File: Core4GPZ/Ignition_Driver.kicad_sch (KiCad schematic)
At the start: 10 parts, among them Q1 IRG4PF50W, Q2 IRG4PF50W

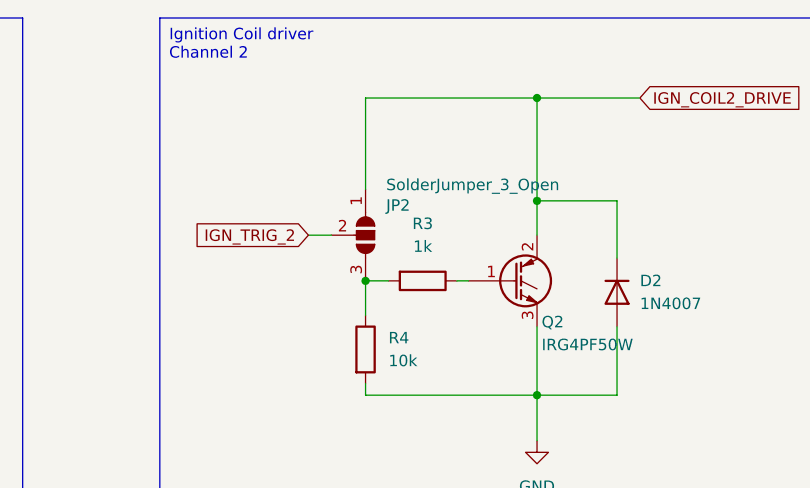
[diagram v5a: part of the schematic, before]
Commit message: Started Implementation of VR Conditionner
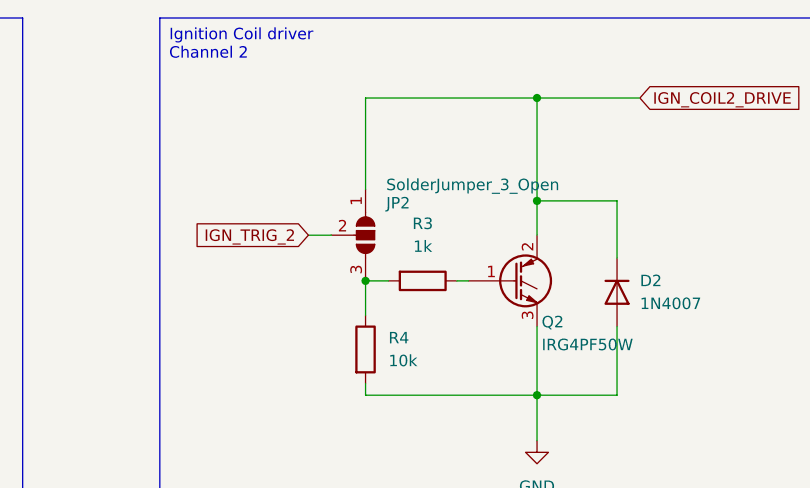
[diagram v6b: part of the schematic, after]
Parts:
- JP1, JP2: footprint (none) -> Jumper:SolderJumper-3_P1.3mm_Open_RoundedPad1.0x1.5mm
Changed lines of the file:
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@@
+	)
+	(junction
+		(at 154.94 60.96)
+		(diameter 0)
+		(color 0 0 0 0)
 	)
 	(junction
@@
 	(junction
 		(at 173.99 73.66)
-		(diameter 0)
-		(color 0 0 0 0)
-	)
-	(junction
-		(at 154.94 60.96)
 		(diameter 0)
 		(color 0 0 0 0)
@@
 	)
 	(symbol
-		(lib_id "Jumper:SolderJumper_3_Open")
-		(at 154.94 55.88 270)
-		(unit 1)
-		(exclude_from_sim yes)
-		(in_bom no)
-		(on_board yes)
-		(dnp no)
-		(property "Reference" "JP2"
-			(at 157.226 52.578 90)
-			(effects
-				(font
-					(size 1.27 1.27)
-				)
-				(justify left)
-			)
-		)
-		(property "Value" "SolderJumper_3_Open"
-			(at 157.226 50.292 90)
-			(effects
-				(font
-					(size 1.27 1.27)
-				)
-				(justify left)
-			)
-		)
-		(property "Footprint" ""
-			(at 154.94 55.88 0)
-			(effects
-				(font
-					(size 1.27 1.27)
-				)
-				(hide yes)
-			)
-		)
-		(property "Datasheet" "~"
-			(at 154.94 55.88 0)
-			(effects
-				(font
-					(size 1.27 1.27)
-				)
-				(hide yes)
-			)
-		)
-		(property "Description" "Solder Jumper, 3-pole, open"
-			(at 154.94 55.88 0)
-			(effects
-				(font
-					(size 1.27 1.27)
-				)
-				(hide yes)
-			)
-		)
-		(pin "3"
-		)
-		(pin "2"
-		)
-		(pin "1"
-		)
-		(instances
-			(project "Core4GPZ"
-				(path "/ac28f42d-34b3-4fcc-84dd-ab6106f99610/d5427090-fd08-4b35-ae6e-bc2a7b0d4087"
-					(reference "JP2")
-					(unit 1)
-				)
-			)
-		)
-	)
-	(symbol
 		(lib_id "power:GND")
 		(at 173.99 78.74 0)
@@
 	(symbol
 		(lib_id "Jumper:SolderJumper_3_Open")
+		(at 154.94 55.88 270)
+		(unit 1)
+		(exclude_from_sim yes)
+		(in_bom no)
+		(on_board yes)
+		(dnp no)
+		(property "Reference" "JP2"
+			(at 157.226 52.324 90)
+			(effects
+				(font
+					(size 1.27 1.27)
+				)
+				(justify left)
+			)
+		)
+		(property "Value" "SolderJumper_3_Open"
+			(at 157.226 50.292 90)
+			(effects
+				(font
+					(size 1.27 1.27)
+				)
+				(justify left)
+			)
+		)
+		(property "Footprint" "Jumper:SolderJumper-3_P1.3mm_Open_RoundedPad1.0x1.5mm"
+			(at 154.94 55.88 0)
+			(effects
+				(font
+					(size 1.27 1.27)
+				)
+				(hide yes)
+			)
+		)
+		(property "Datasheet" "~"
+			(at 154.94 55.88 0)
+			(effects
+				(font
+					(size 1.27 1.27)
+				)
+				(hide yes)
+			)
+		)
+		(property "Description" "Solder Jumper, 3-pole, open"
+			(at 154.94 55.88 0)
+			(effects
+				(font
+					(size 1.27 1.27)
+				)
+				(hide yes)
+			)
+		)
+		(pin "3"
+		)
+		(pin "2"
+		)
+		(pin "1"
+		)
+		(instances
+			(project "Core4GPZ"
+				(path "/ac28f42d-34b3-4fcc-84dd-ab6106f99610/d5427090-fd08-4b35-ae6e-bc2a7b0d4087"
+					(reference "JP2")
+					(unit 1)
+				)
+			)
+		)
+	)
+	(symbol
+		(lib_id "Jumper:SolderJumper_3_Open")
 		(at 69.85 55.88 270)
 		(unit 1)
@@
 			)
 		)
-		(property "Footprint" ""
+		(property "Footprint" "Jumper:SolderJumper-3_P1.3mm_Open_RoundedPad1.0x1.5mm"
 			(at 69.85 55.88 0)
 			(effects

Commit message: Tiny modification
???
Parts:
- D1, D2: footprint Diode_THT:D_DO-41_SOD81_P2.54mm_Vertical_KathodeUp -> Diode_THT:D_DO-41_SOD81_P7.62mm_Horizontal
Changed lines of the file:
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@@
+	)
+	(symbol
+		(lib_id "Device:D")
+		(at 182.88 62.23 270)
+		(unit 1)
+		(exclude_from_sim no)
+		(in_bom yes)
+		(on_board yes)
+		(dnp no)
+		(fields_autoplaced yes)
+		(property "Reference" "D2"
+			(at 185.42 60.9599 90)
+			(effects
+				(font
+					(size 1.27 1.27)
+				)
+				(justify left)
+			)
+		)
+		(property "Value" "1N4007"
+			(at 185.42 63.4999 90)
+			(effects
+				(font
+					(size 1.27 1.27)
+				)
+				(justify left)
+			)
+		)
+		(property "Footprint" "Diode_THT:D_DO-41_SOD81_P7.62mm_Horizontal"
+			(at 182.88 62.23 0)
+			(effects
+				(font
+					(size 1.27 1.27)
+				)
+				(hide yes)
+			)
+		)
+		(property "Datasheet" "~"
+			(at 182.88 62.23 0)
+			(effects
+				(font
+					(size 1.27 1.27)
+				)
+				(hide yes)
+			)
+		)
+		(property "Description" ""
+			(at 182.88 62.23 0)
+			(effects
+				(font
+					(size 1.27 1.27)
+				)
+				(hide yes)
+			)
+		)
+		(property "Sim.Device" "D"
+			(at 182.88 62.23 0)
+			(effects
+				(font
+					(size 1.27 1.27)
+				)
+				(hide yes)
+			)
+		)
+		(property "Sim.Pins" "1=K 2=A"
+			(at 182.88 62.23 0)
+			(effects
+				(font
+					(size 1.27 1.27)
+				)
+				(hide yes)
+			)
+		)
+		(pin "2"
+		)
+		(pin "1"
+		)
+		(instances
+			(project "Core4GPZ"
+				(path "/ac28f42d-34b3-4fcc-84dd-ab6106f99610/d5427090-fd08-4b35-ae6e-bc2a7b0d4087"
+					(reference "D2")
+					(unit 1)
+				)
+			)
+		)
 	)
 	(symbol
@@
 	)
 	(symbol
-		(lib_id "Device:D")
-		(at 182.88 62.23 270)
-		(unit 1)
-		(exclude_from_sim no)
-		(in_bom yes)
-		(on_board yes)
-		(dnp no)
-		(fields_autoplaced yes)
-		(property "Reference" "D2"
-			(at 185.42 60.9599 90)
-			(effects
-				(font
-					(size 1.27 1.27)
-				)
-				(justify left)
-			)
-		)
-		(property "Value" "1N4007"
-			(at 185.42 63.4999 90)
-			(effects
-				(font
-					(size 1.27 1.27)
-				)
-				(justify left)
-			)
-		)
-		(property "Footprint" "Diode_THT:D_DO-41_SOD81_P2.54mm_Vertical_KathodeUp"
-			(at 182.88 62.23 0)
-			(effects
-				(font
-					(size 1.27 1.27)
-				)
-				(hide yes)
-			)
-		)
-		(property "Datasheet" "~"
-			(at 182.88 62.23 0)
-			(effects
-				(font
-					(size 1.27 1.27)
-				)
-				(hide yes)
-			)
-		)
-		(property "Description" ""
-			(at 182.88 62.23 0)
-			(effects
-				(font
-					(size 1.27 1.27)
-				)
-				(hide yes)
-			)
-		)
-		(property "Sim.Device" "D"
-			(at 182.88 62.23 0)
-			(effects
-				(font
-					(size 1.27 1.27)
-				)
-				(hide yes)
-			)
-		)
-		(property "Sim.Pins" "1=K 2=A"
-			(at 182.88 62.23 0)
-			(effects
-				(font
-					(size 1.27 1.27)
-				)
-				(hide yes)
-			)
-		)
-		(pin "2"
-		)
-		(pin "1"
-		)
-		(instances
-			(project "Core4GPZ"
-				(path "/ac28f42d-34b3-4fcc-84dd-ab6106f99610/d5427090-fd08-4b35-ae6e-bc2a7b0d4087"
-					(reference "D2")
-					(unit 1)
-				)
-			)
-		)
-	)
-	(symbol
 		(lib_id "Device:R")
 		(at 161.29 60.96 270)
@@
 			)
 		)
-		(property "Footprint" "Diode_THT:D_DO-41_SOD81_P2.54mm_Vertical_KathodeUp"
+		(property "Footprint" "Diode_THT:D_DO-41_SOD81_P7.62mm_Horizontal"
 			(at 97.79 62.23 0)
 			(effects
